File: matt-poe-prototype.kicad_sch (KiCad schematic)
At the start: 53 parts, among them J2 Conn_02x02_Odd_Even, T1 EP475SG-10, U2 MP8017GL-Z, U4 AP62250WU-7

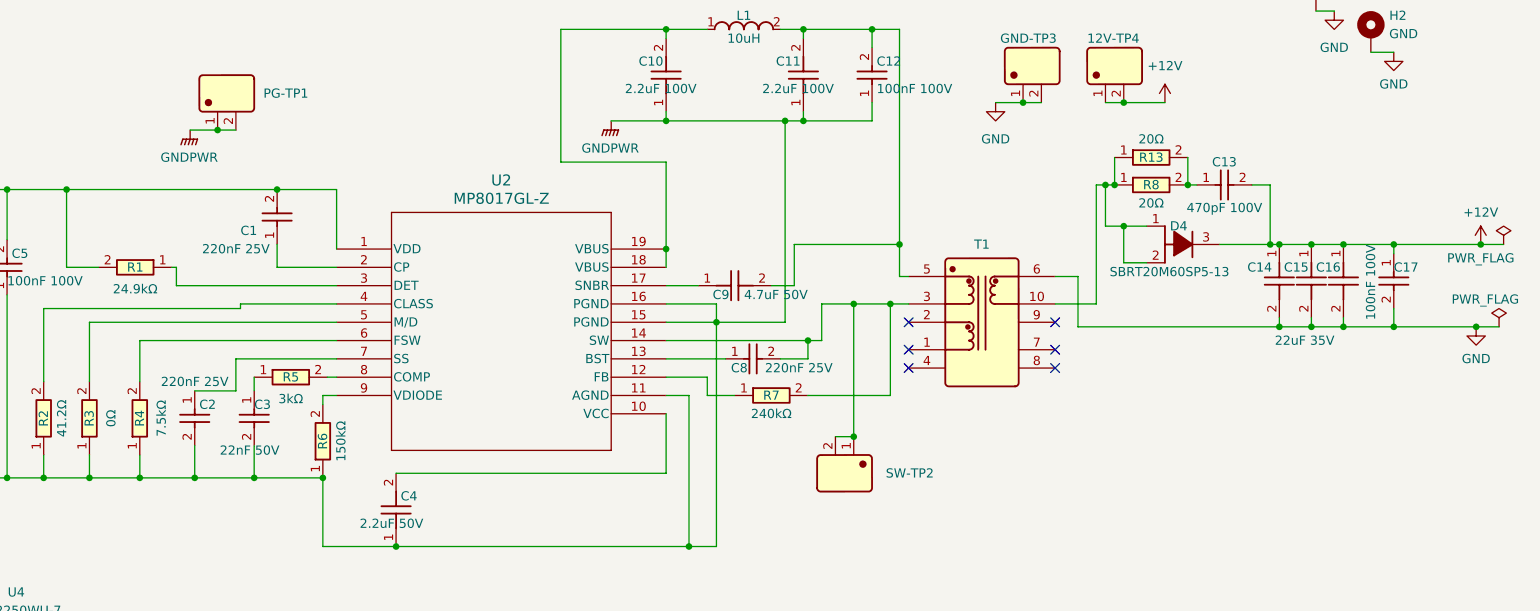
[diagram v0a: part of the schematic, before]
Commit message: Some component substitutions for optimization and for part availability.
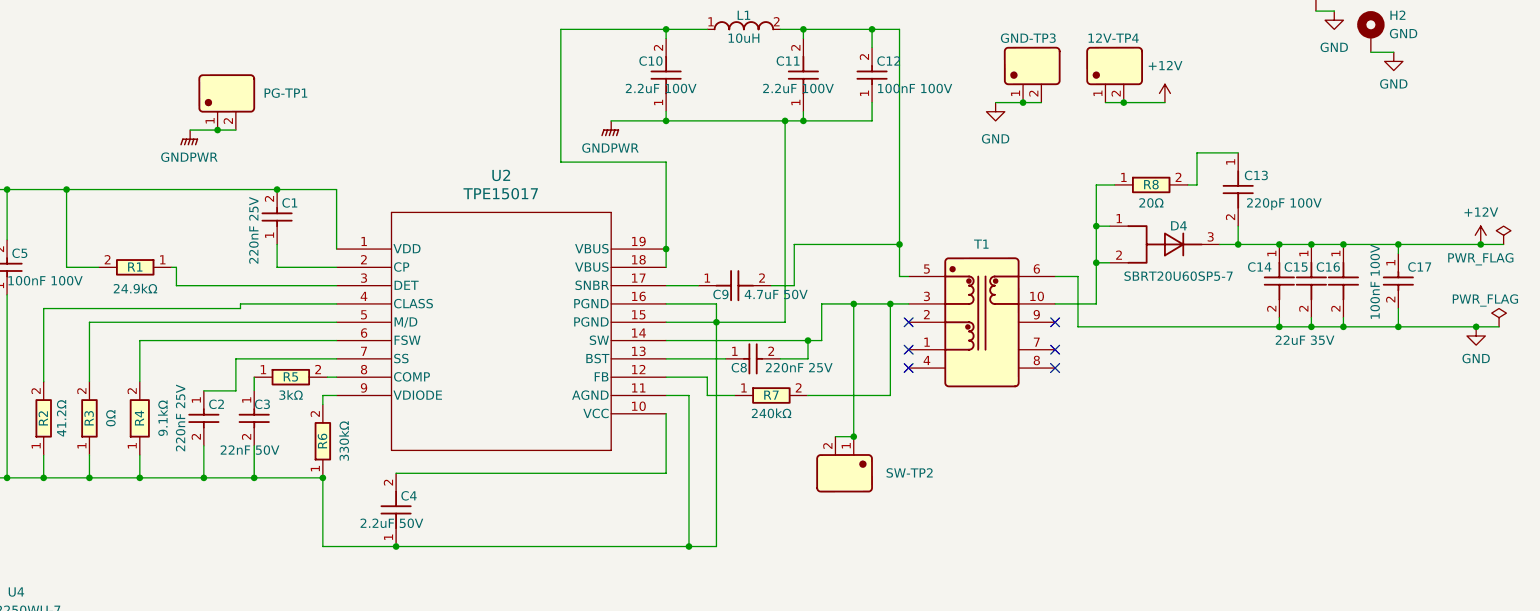
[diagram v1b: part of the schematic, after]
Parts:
- removed R13: 20Ω, JLCImport:R_1206_C17903, symbol JLCImport:1206W4F100JT5E
- C13: value 470pF 100V -> 220pF 100V; footprint JLCImport:C_0603_C107062 -> JLCImport:GCM1885C2A221JA16D; symbol JLCImport:CC0603KRX7R0BB471 -> JLCImport:GCM1885C2A221JA16D; LCSC C107062 -> C388907; Manufacturer YAGEO -> Murata Electronics; Manufacturer Part CC0603KRX7R0BB471 -> GCM1885C2A221JA16D
- D4: value SBRT20M60SP5-13 -> SBRT20U60SP5-7; footprint JLCImport:D_POWERDI5_C5245040 -> JLCImport:SBRT20U60SP5-7; symbol JLCImport:SBRT20M60SP5-13 -> JLCImport:SBRT20U60SP5-7; LCSC C5245040 -> C156299; Manufacturer Part SBRT20M60SP5-13 -> SBRT20U60SP5-7
- R4: value 7.5kΩ -> 9.1kΩ; footprint JLCImport:R_0603_C23234 -> JLCImport:FRC0603J912_TS; symbol JLCImport:0603WAF7501T5E -> JLCImport:FRC0603J912_TS; LCSC C23234 -> C2907210; MPN 560112116080 -> (none); Manufacturer UNI-ROYAL(Uniroyal Elec) -> FOJAN; Manufacturer Part 0603WAF7501T5E -> FRC0603J912 TS
- R6: value 150kΩ -> 330kΩ; footprint JLCImport:R_0603_C22807 -> JLCImport:0603WAF3303T5E; symbol JLCImport:0603WAF1503T5E -> JLCImport:0603WAF3303T5E; LCSC C22807 -> C23137; Manufacturer Part 0603WAF1503T5E -> 0603WAF3303T5E
- U2: value MP8017GL-Z -> TPE15017; symbol MPS:MP8017GL-Z -> MPS:TPE15017; ALT Manufacturer (none) -> Monolithic Power Systems; ALTMPN (none) -> MP8017GL-Z; MPN MP8017GL-Z -> TPE15017; Manufacturer (none) -> 3Peak
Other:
- moved on the sheet: C13, C17, C2

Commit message: Updating BOM and BOM formatting
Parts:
- C6, C7: Manufacturer (none) -> Murata Electronics
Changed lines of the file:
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@@
 			)
 		)
-		(property "Manufacturer" ""
+		(property "Manufacturer" "Murata Electronics"
 			(at 26.035 62.865 0)
 			(hide yes)
@@
 			)
 		)
-		(property "Manufacturer" ""
+		(property "Manufacturer" "Murata Electronics"
 			(at 26.035 56.515 0)
 			(hide yes)
